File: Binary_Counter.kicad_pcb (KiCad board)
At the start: 2 copper layers, 100 x 15 mm, 34 parts, among them J2 Conn_01x03_Pin, SW2 SW_MEC_5E, U1 CH32V003FxUx

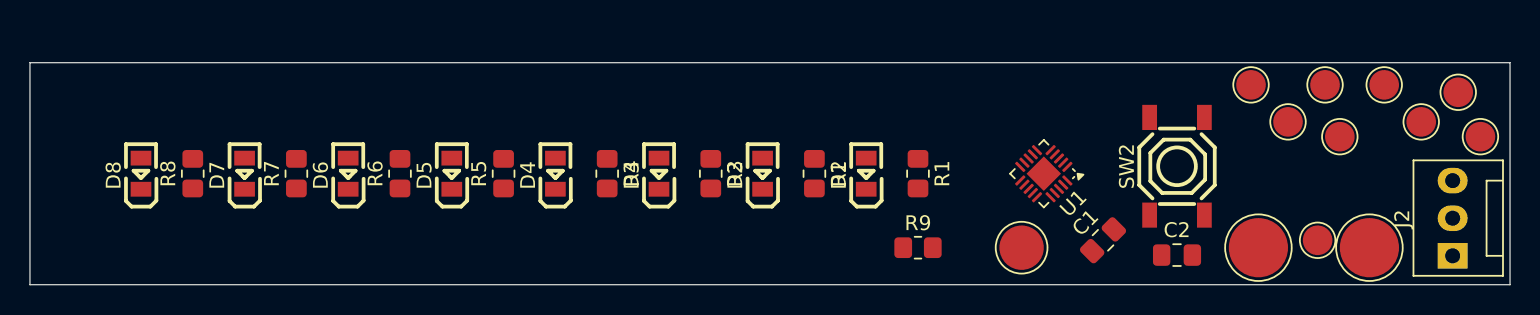
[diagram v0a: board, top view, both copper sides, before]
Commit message: complete routing
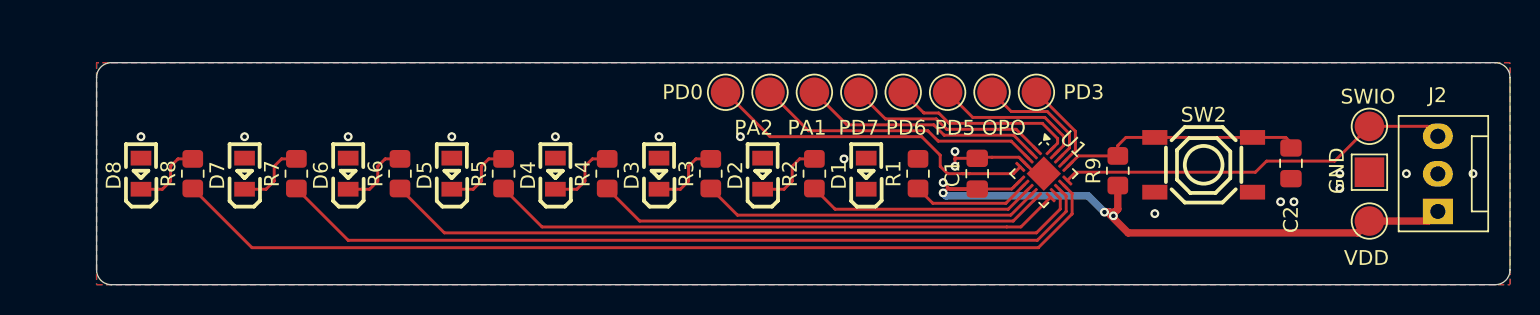
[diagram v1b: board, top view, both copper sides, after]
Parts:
- removed TP11: SWIO, TestPoint:TestPoint_Pad_D2.0mm
- TP1: value SWIO -> VDD; footprint TestPoint:TestPoint_Pad_D3.0mm -> TestPoint:TestPoint_Pad_D2.0mm
- TP2: value VDD -> SWIO; footprint TestPoint:TestPoint_Pad_D4.0mm -> TestPoint:TestPoint_Pad_D2.0mm
- TP3: footprint TestPoint:TestPoint_Pad_D4.0mm -> TestPoint:TestPoint_Pad_2.0x2.0mm
- TP5: value PD4 -> OPO
- moved TP12 35.5 mm to (165.5, 87.5)
- moved TP10 35.1 mm to (168.5, 87.5)
- moved TP9 34.5 mm to (171.5, 87.5)
- moved TP8 32.6 mm to (174.5, 87.5)
- moved TP7 32.5 mm to (177.5, 87.5)
- moved TP6 32.1 mm to (180.5, 87.5)
- moved TP5 31.5 mm to (183.5, 87.5)
- moved TP4 30.1 mm to (186.5, 87.5)
- moved TP1 23.6 mm to (209.0, 96.2)
- moved R9 14.5 mm to (192.0, 92.8), turned to 90 degrees
- moved TP2 11.1 mm to (209.0, 89.8)
- moved C2 9.89 mm to (203.7, 92.3), turned to -90 degrees
- moved C1 9.62 mm to (182.5, 93.0), turned to 90 degrees
- moved TP3 5.10 mm to (209.0, 92.9)
- moved J2 3.16 mm to (213.6, 95.5)
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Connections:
- J2 pad 1: /SWIO -> VDD
- J2 pad 3: VDD -> /SWIO
- TP1 pad 1: /SWIO -> VDD
- TP2 pad 1: VDD -> /SWIO
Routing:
- net /mLED8: track 0.00 -> 64.2 mm
- net /mLED7: track 0.00 -> 56.0 mm
- net /mLED6: track 0.00 -> 47.8 mm
- net VDD: track 0.00 -> 46.5 mm, vias 0 -> 4
- net /mLED5: track 0.00 -> 38.9 mm
- net /mLED4: track 0.00 -> 30.6 mm
- net /SWIO: track 0.00 -> 26.8 mm
- net Net-(U1-PD0): track 0.00 -> 23.3 mm
- net /mLED3: track 0.00 -> 23.1 mm
- net Net-(U1-PA2): track 0.00 -> 19.3 mm
- net Net-(U1-PD2): track 0.00 -> 16.9 mm
- net Net-(U1-PA1): track 0.00 -> 16.5 mm
- net /mLED2: track 0.00 -> 15.6 mm
- net Net-(U1-PD7): track 0.00 -> 13.7 mm
- net Net-(U1-PD6): track 0.00 -> 12.7 mm
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- added copper zone on B.Cu, net GND
- added copper zone on F.Cu, net GND
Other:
- board size 100 x 15 mm -> 95.5 x 15 mm

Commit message: add revision to silk
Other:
- board text added: "@shannietron"
- board text added: "binary_counter v1"
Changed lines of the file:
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@@
 		(layer "Edge.Cuts")
+	)
+	(gr_text "binary_counter v1"
+		(at 140.6 87.9 0)
+		(layer "F.Fab")
+		(effects
+			(font
+				(size 1 1)
+				(thickness 0.15)
+			)
+			(justify left bottom)
+		)
+	)
+	(gr_text "@shannietron"
+		(at 127.8 88 0)
+		(layer "F.Fab")
+		(effects
+			(font
+				(size 1 1)
+				(thickness 0.15)
+			)
+			(justify left bottom)
+		)
 	)
 	(segment

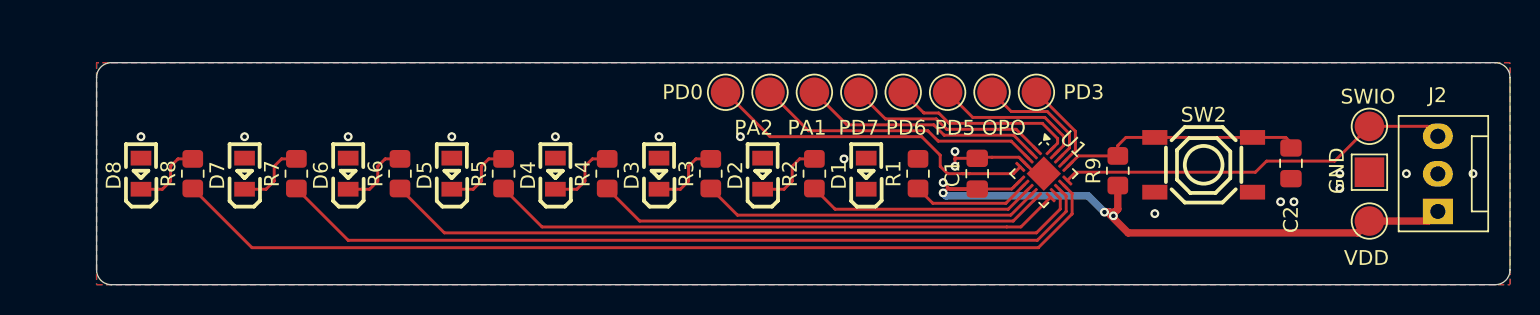
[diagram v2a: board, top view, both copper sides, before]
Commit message: add M2 mounting holes
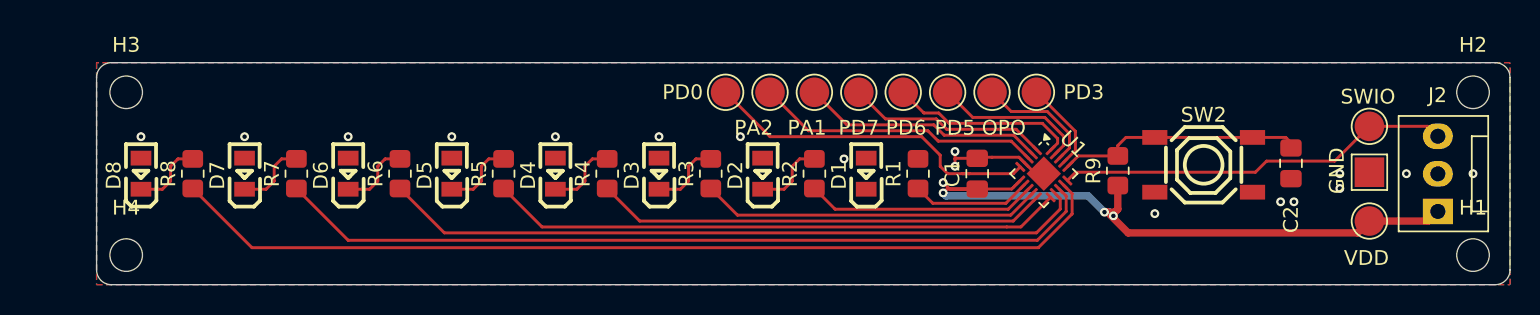
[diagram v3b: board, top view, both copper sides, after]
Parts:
- added H1: MountingHole_Pad, MountingHole:MountingHole_2.2mm_M2, F.Cu at (216.0, 98.5)
- added H2: MountingHole_Pad, MountingHole:MountingHole_2.2mm_M2, F.Cu at (216.0, 87.5)
- added H3: MountingHole_Pad, MountingHole:MountingHole_2.2mm_M2, F.Cu at (125.0, 87.5)
- added H4: MountingHole_Pad, MountingHole:MountingHole_2.2mm_M2, F.Cu at (125.0, 98.5)

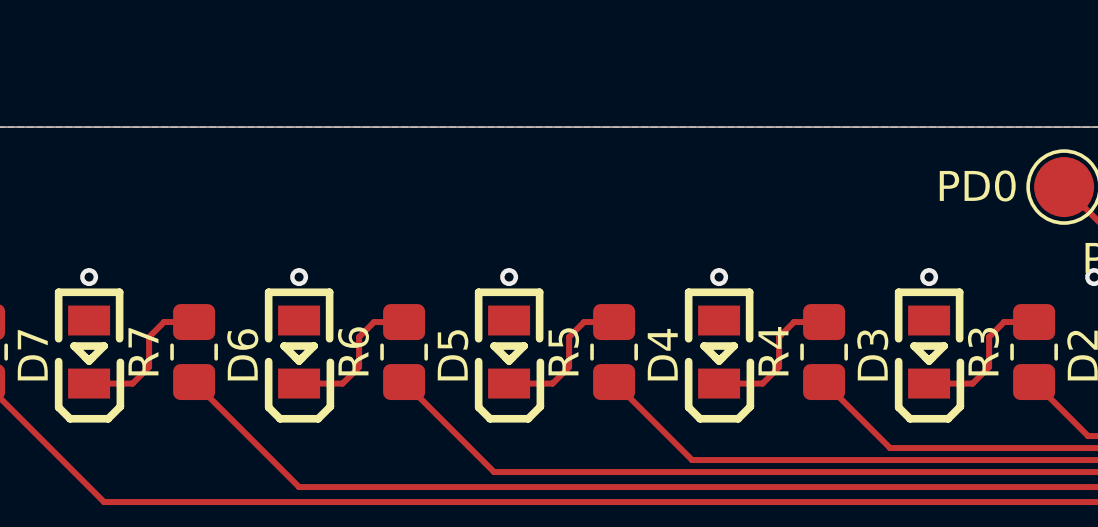
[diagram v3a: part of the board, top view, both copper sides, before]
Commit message: add url to back silk
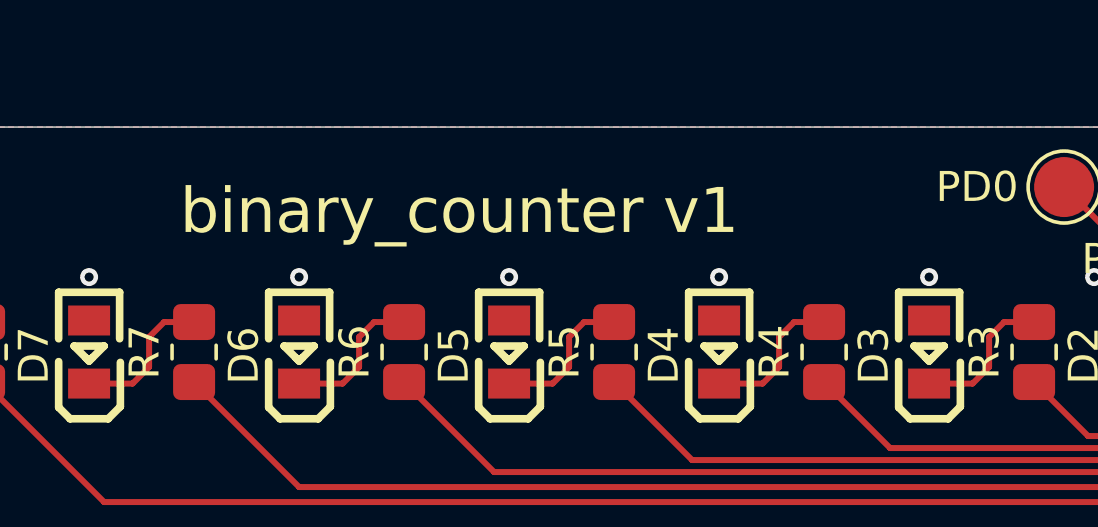
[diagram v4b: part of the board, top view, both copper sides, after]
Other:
- board text added: "shan.mp/binary_counter"
- board text removed: "@shannietron"

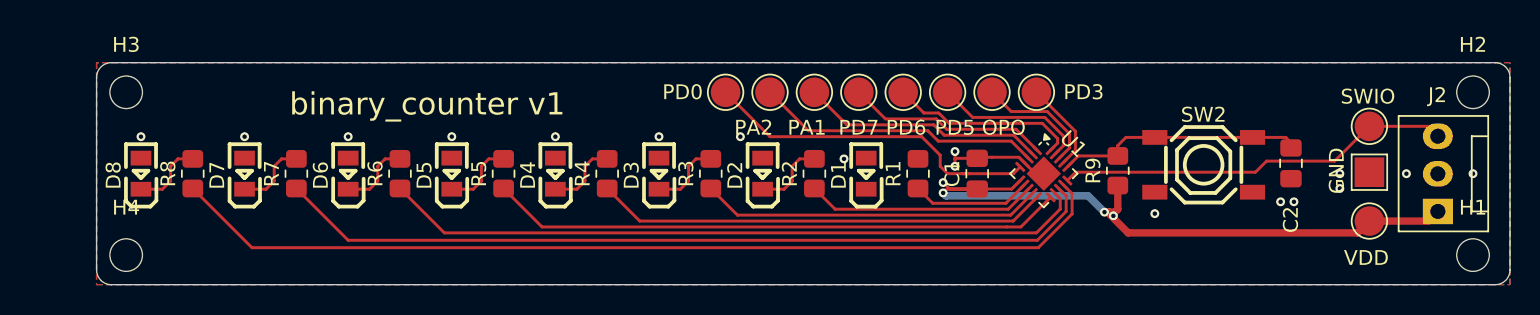
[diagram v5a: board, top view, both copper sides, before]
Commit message: place and route LDO
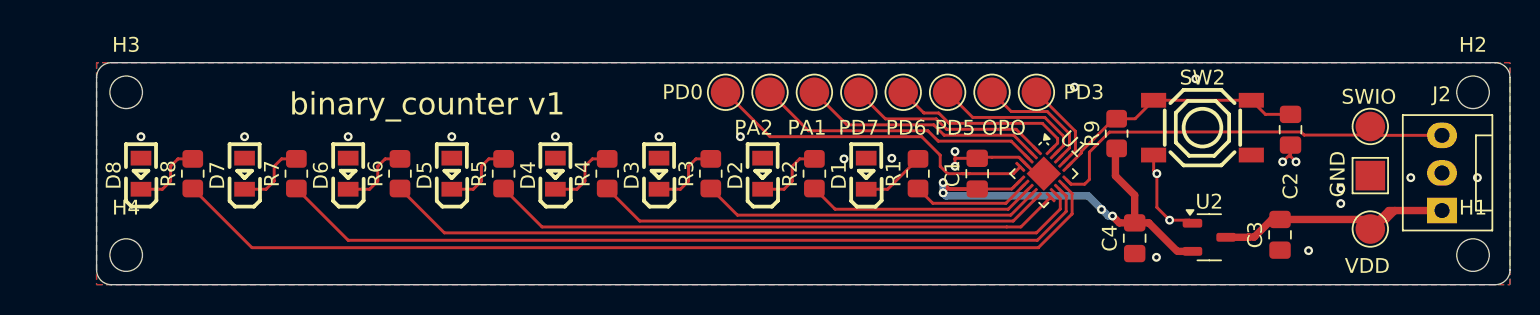
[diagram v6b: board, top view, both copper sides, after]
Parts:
- added C3: 1uF, Capacitor_SMD:C_0805_2012Metric_Pad1.18x1.45mm_HandSolder, F.Cu at (203.0, 97.1)
- added C4: 1uF, Capacitor_SMD:C_0805_2012Metric_Pad1.18x1.45mm_HandSolder, F.Cu at (193.1, 97.4)
- added U2: XC6206PxxxMR, Package_TO_SOT_SMD:SOT-23-3, F.Cu at (198.2, 97.3)
- moved SW2 2.51 mm to (197.7, 89.9)
- moved R9 2.51 mm to (191.9, 90.3)
- moved C2 2.27 mm to (203.7, 90.0)
- moved TP1 0.54 mm to (209.1, 96.7)
- moved J2 0.29 mm to (213.9, 95.5)
- moved TP3 0.24 mm to (209.1, 93.1)
- moved TP2 0.06 mm to (209.1, 89.8)
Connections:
- J2 pad 1: VDD -> VBAT
- TP1 pad 1: VDD -> VBAT
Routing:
- net VBAT: track 0.00 -> 17.5 mm
- net VDD: track 46.5 -> 32.8 mm
- net GND: track 7.51 -> 16.8 mm, vias 17 -> 23
- net /LED1: track 0.00 -> 4.35 mm
- net /SWIO: track 26.8 -> 28.6 mm
- net Net-(U1-PD2): track 16.9 -> 17.4 mm

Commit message: add design rules from jlc template, fix errors
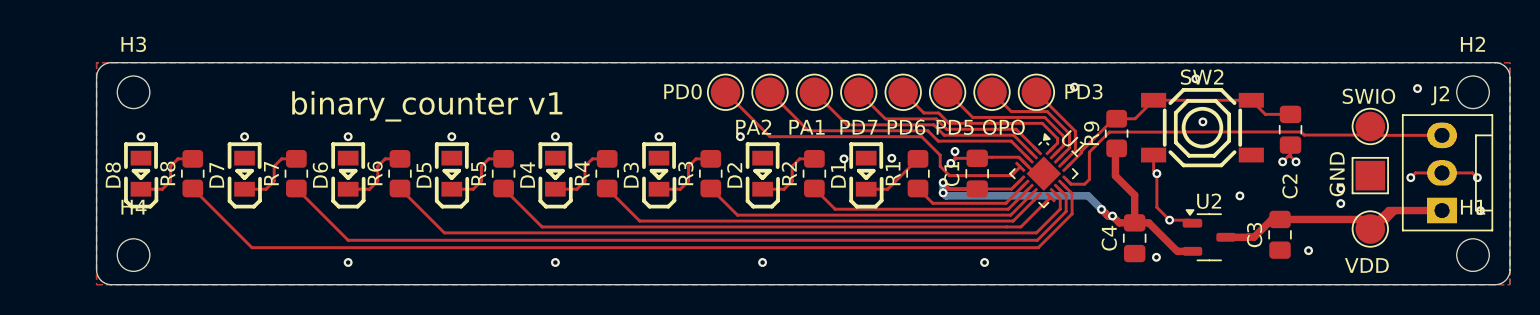
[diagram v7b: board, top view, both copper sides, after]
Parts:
- moved H3 0.50 mm to (125.5, 87.5)
- moved H4 0.50 mm to (125.5, 98.5)
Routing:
- net GND: track 16.8 -> 21.5 mm, vias 23 -> 31
- net VDD: track 32.8 -> 33.7 mm
